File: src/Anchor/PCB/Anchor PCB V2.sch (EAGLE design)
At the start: 39 parts, among them IC1 DWM1000, IC3 ENC28J60-I_SS, J1 SI-50154-F, J2 ISP PROG 1, J3 ISP PROG 2, J4 POWER_JACK, Y1 8MHz, Y2 8MHz, Y3 25MHz

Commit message: Edited Anchor PCB schematic + Board V1
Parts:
- removed IC1: DWM1000, DWM1000:DWM1000
- added C10, C11: 100nF, rcl:C-EUC0805
- added D1: POWER, SparkFun-LED:LED-BLUE1206
- added D2: STATUS, SparkFun-LED:LED-RED1206
- added D3: TX, SparkFun-LED:LED-YELLOWLILYPAD
- added D4: RX, SparkFun-LED:LED-GREEN1206
- added D5: DWM-TX, SparkFun-LED:LED-YELLOWLILYPAD
- added D6: DWM-RX, SparkFun-LED:LED-GREEN1206
- added H1, H2, H3, H4: MOUNT-HOLE3.0, holes:MOUNT-HOLE3.0
- added L1: FB_1206, rc-master-smd:FB_1206
- added R17: 470, rcl:R-EU_R1206
- added R18, R22: 220, rcl:R-EU_R1206
- added R19, R21: 270, rcl:R-EU_R1206
- added R20: 390, rcl:R-EU_R1206
- added U$2: DWM1000, Eigen Library:DWM1000-BREAKOUT
- added UART1: UART1, Eigen Library:UART-6PIN
- added UART2: UART2, Eigen Library:UART-6PIN
- C1, C2: value 0.1uF -> 100nF; device rcl:C-EUC1206 -> rcl:C-EUC0805
- C3, C4, C5, C6, C7, C8, C9: device rcl:C-EUC1206 -> rcl:C-EUC0805
- R1, R11, R12, R13, R14, R15, R16, R2, R7, R8, R9: device rcl:R-EU_R1206 -> rcl:R-EU_R0805
- R3, R4, R5, R6: value 50 -> 49.9
- S2: value RESET 1 -> RESET 2
- U$1: value DC-DC-STEP-DOWN-LM2596 -> DC-STEPDOWN
- Y1, Y2, Y3: device SparkFun-Clocks:CRYSTALPTH-HC49US -> SparkFun-Clocks:CRYSTALSMD-HC49UP
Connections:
- removed net E-INT: IC3.~INT, MCU1.PD2_[PCINT18]
- new net DTR1: C10.1, UART1.DTR
- new net DTR2: C11.1, UART2.DTR
- new net DW-RXLED: R22.2, U$2.RXLED
- new net DW-TXLED: R21.2, U$2.TXLED
- new net N$19: UART1.CTS
- new net N$20: D5.A, R21.1
- new net N$21: D4.A, R18.1
- new net N$22: D2.A, R20.1
- new net N$23: UART2.CTS
- new net N$24: D3.A, R19.1
- new net N$25: D6.A, R22.1
- new net N$26: D1.A, R17.1
- new net RX1: MCU1.PD0_[PCINT16], UART1.TXD
- new net RX2: MCU2.PD0_[PCINT16], UART2.TXD
- new net RX3: D4.C, MCU1.PC2_[PCINT10], MCU2.PC3_[PCINT11]
- new net STATUS: D2.C, MCU1.PC1_[PCINT9]
- new net TX1: MCU1.PD1_[PCINT17], UART1.RXD
- new net TX2: MCU2.PD1_[PCINT17], UART2.RXD
- new net TX3: D3.C, MCU1.PC3_[PCINT11], MCU2.PC2_[PCINT10]
- net CS2: now also U$2.CS; no longer IC1.SPICSN
- net DW-RST: now also U$2.RST; no longer IC1.RSTN
- net GND: now also D1.C, D5.C, D6.C, U$2.GND, UART1.GND, UART2.GND; no longer IC1.VSS_1, IC1.VSS_2, IC1.VSS_3, IC1.VSS_4, IC1.VSS_5
- net IRQ: now also U$2.IRQ; no longer IC1.IRQ/GPIO8
- net MOSI2: now also R16.1; no longer R14.1
- net N$13: now also L1.2
- net N$16: now also U$2.CLK; no longer IC1.SPIMOSI
- net N$17: now also U$2.MISO; no longer IC1.SPIMISO
- net N$18: now also U$2.MOSI; no longer IC1.SPICLK
- net RST1: now also C10.2
- net RST2: now also C11.2
- net SCK2: now also R14.1; no longer R16.1
- net VCC: now also L1.1, R17.2, R18.2, R19.2, R20.2, U$2.VCC; no longer IC1.VDD3V3_1, IC1.VDD3V3_2, IC1.VDDAON
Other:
- moved on the sheet: C7, C8, C9, IC3, R10, R11, R12, R13, R14, R15, R16, R7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

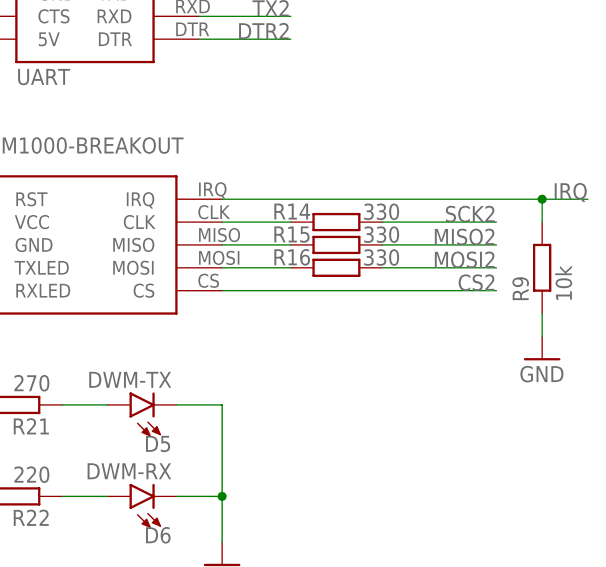
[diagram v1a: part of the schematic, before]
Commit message: Removed some unnecessary resistors in Anchor V2
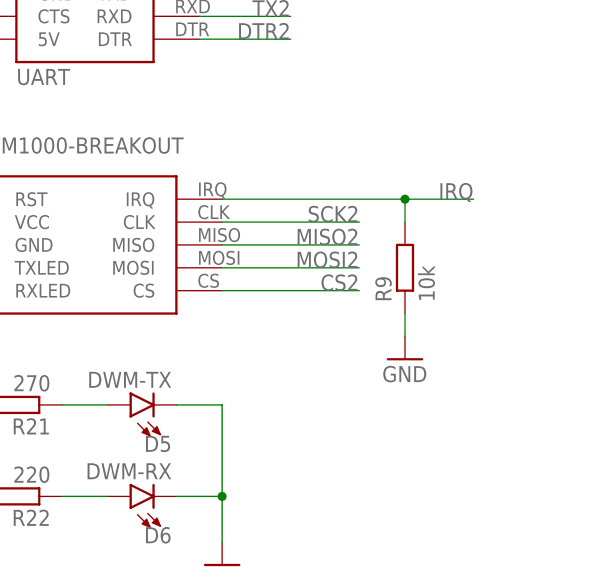
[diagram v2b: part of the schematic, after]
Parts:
- removed R14, R15, R16: 330, rcl:R-EU_R0805
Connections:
- removed net N$16: R14.2, U$2.CLK
- removed net N$17: R15.2, U$2.MISO
- removed net N$18: R16.2, U$2.MOSI
- net MISO2: now also U$2.MISO; no longer R15.1
- net MOSI2: now also U$2.MOSI; no longer R16.1
- net SCK2: now also U$2.CLK; no longer R14.1
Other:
- moved on the sheet: R9
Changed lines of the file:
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@@
 <part name="R12" library="rcl" library_urn="urn:adsk.eagle:library:334" deviceset="R-EU_" device="R0805" package3d_urn="urn:adsk.eagle:package:23553/2" value="330"/>
 <part name="R13" library="rcl" library_urn="urn:adsk.eagle:library:334" deviceset="R-EU_" device="R0805" package3d_urn="urn:adsk.eagle:package:23553/2" value="330"/>
-<part name="R14" library="rcl" library_urn="urn:adsk.eagle:library:334" deviceset="R-EU_" device="R0805" package3d_urn="urn:adsk.eagle:package:23553/2" value="330"/>
-<part name="R15" library="rcl" library_urn="urn:adsk.eagle:library:334" deviceset="R-EU_" device="R0805" package3d_urn="urn:adsk.eagle:package:23553/2" value="330"/>
-<part name="R16" library="rcl" library_urn="urn:adsk.eagle:library:334" deviceset="R-EU_" device="R0805" package3d_urn="urn:adsk.eagle:package:23553/2" value="330"/>
 <part name="J4" library="SparkFun-Connectors" deviceset="POWER_JACK" device=""/>
 <part name="U$1" library="1484249208697-powermodules" deviceset="DC-DC-STEP-DOWN-LM2596" device="" value="DC-STEPDOWN"/>
@@
 <attribute name="VALUE" x="322.58" y="78.74" size="1.778" layer="96"/>
 </instance>
-<instance part="R9" gate="G$1" x="497.84" y="137.16" rot="R90">
-<attribute name="NAME" x="496.3414" y="133.35" size="1.778" layer="95" rot="R90"/>
-<attribute name="VALUE" x="501.142" y="133.35" size="1.778" layer="96" rot="R90"/>
-</instance>
-<instance part="GND10" gate="1" x="497.84" y="127">
-<attribute name="VALUE" x="495.3" y="124.46" size="1.778" layer="96"/>
+<instance part="R9" gate="G$1" x="482.6" y="137.16" rot="R90">
+<attribute name="NAME" x="481.1014" y="133.35" size="1.778" layer="95" rot="R90"/>
+<attribute name="VALUE" x="485.902" y="133.35" size="1.778" layer="96" rot="R90"/>
+</instance>
+<instance part="GND10" gate="1" x="482.6" y="127">
+<attribute name="VALUE" x="480.06" y="124.46" size="1.778" layer="96"/>
 </instance>
 <instance part="C7" gate="G$1" x="10.16" y="116.84" rot="R180">
@@
 <attribute name="NAME" x="43.18" y="108.7374" size="1.778" layer="95" rot="R180"/>
 <attribute name="VALUE" x="32.512" y="108.712" size="1.778" layer="96" rot="R180"/>
-</instance>
-<instance part="R14" gate="G$1" x="474.98" y="142.24" rot="R180">
-<attribute name="NAME" x="472.186" y="144.2974" size="1.778" layer="95" rot="R180"/>
-<attribute name="VALUE" x="482.092" y="144.272" size="1.778" layer="96" rot="R180"/>
-</instance>
-<instance part="R15" gate="G$1" x="474.98" y="139.7" rot="R180">
-<attribute name="NAME" x="472.186" y="141.7574" size="1.778" layer="95" rot="R180"/>
-<attribute name="VALUE" x="482.092" y="141.732" size="1.778" layer="96" rot="R180"/>
-</instance>
-<instance part="R16" gate="G$1" x="474.98" y="137.16" rot="R180">
-<attribute name="NAME" x="472.186" y="139.2174" size="1.778" layer="95" rot="R180"/>
-<attribute name="VALUE" x="482.092" y="139.192" size="1.778" layer="96" rot="R180"/>
 </instance>
 <instance part="J4" gate="G$1" x="60.96" y="157.48">
@@
 <pinref part="GND10" gate="1" pin="GND"/>
 <pinref part="R9" gate="G$1" pin="1"/>
-<wire x1="497.84" y1="129.54" x2="497.84" y2="132.08" width="0.1524" layer="91"/>
+<wire x1="482.6" y1="129.54" x2="482.6" y2="132.08" width="0.1524" layer="91"/>
 </segment>
 <segment>
@@
 </segment>
 <segment>
-<pinref part="R16" gate="G$1" pin="1"/>
-<wire x1="480.06" y1="137.16" x2="492.76" y2="137.16" width="0.1524" layer="91"/>
-<label x="492.76" y="137.16" size="1.778" layer="95" rot="MR0"/>
+<label x="477.52" y="137.16" size="1.778" layer="95" rot="MR0"/>
+<pinref part="U$2" gate="G$1" pin="MOSI"/>
+<wire x1="462.28" y1="137.16" x2="477.52" y2="137.16" width="0.1524" layer="91"/>
 </segment>
 </net>
@@
 </segment>
 <segment>
-<pinref part="R15" gate="G$1" pin="1"/>
-<wire x1="480.06" y1="139.7" x2="492.76" y2="139.7" width="0.1524" layer="91"/>
-<label x="492.76" y="139.7" size="1.778" layer="95" rot="MR0"/>
+<label x="477.52" y="139.7" size="1.778" layer="95" rot="MR0"/>
+<pinref part="U$2" gate="G$1" pin="MISO"/>
+<wire x1="462.28" y1="139.7" x2="477.52" y2="139.7" width="0.1524" layer="91"/>
 </segment>
 </net>
@@
 </segment>
 <segment>
-<pinref part="R14" gate="G$1" pin="1"/>
-<wire x1="480.06" y1="142.24" x2="492.76" y2="142.24" width="0.1524" layer="91"/>
-<label x="492.76" y="142.24" size="1.778" layer="95" rot="MR0"/>
+<label x="477.52" y="142.24" size="1.778" layer="95" rot="MR0"/>
+<pinref part="U$2" gate="G$1" pin="CLK"/>
+<wire x1="462.28" y1="142.24" x2="477.52" y2="142.24" width="0.1524" layer="91"/>
 </segment>
 </net>
@@
 <segment>
 <pinref part="U$2" gate="G$1" pin="IRQ"/>
-<wire x1="462.28" y1="144.78" x2="497.84" y2="144.78" width="0.1524" layer="91"/>
+<wire x1="462.28" y1="144.78" x2="482.6" y2="144.78" width="0.1524" layer="91"/>
 <pinref part="R9" gate="G$1" pin="2"/>
-<wire x1="497.84" y1="142.24" x2="497.84" y2="144.78" width="0.1524" layer="91"/>
-<junction x="497.84" y="144.78"/>
-<wire x1="497.84" y1="144.78" x2="502.92" y2="144.78" width="0.1524" layer="91"/>
-<label x="502.92" y="144.78" size="1.778" layer="95" rot="MR0"/>
+<wire x1="482.6" y1="142.24" x2="482.6" y2="144.78" width="0.1524" layer="91"/>
+<junction x="482.6" y="144.78"/>
+<wire x1="482.6" y1="144.78" x2="490.22" y2="144.78" width="0.1524" layer="91"/>
+<label x="490.22" y="144.78" size="1.778" layer="95" rot="MR0"/>
 </segment>
 </net>
@@
 <segment>
 <pinref part="U$2" gate="G$1" pin="CS"/>
-<wire x1="462.28" y1="134.62" x2="492.76" y2="134.62" width="0.1524" layer="91"/>
-<label x="492.76" y="134.62" size="1.778" layer="95" rot="MR0"/>
+<wire x1="462.28" y1="134.62" x2="477.52" y2="134.62" width="0.1524" layer="91"/>
+<label x="477.52" y="134.62" size="1.778" layer="95" rot="MR0"/>
 </segment>
 </net>
@@
 </segment>
 </net>
-<net name="N$16" class="0">
-<segment>
-<pinref part="R14" gate="G$1" pin="2"/>
-<pinref part="U$2" gate="G$1" pin="CLK"/>
-<wire x1="469.9" y1="142.24" x2="462.28" y2="142.24" width="0.1524" layer="91"/>
-</segment>
-</net>
-<net name="N$17" class="0">
-<segment>
-<pinref part="R15" gate="G$1" pin="2"/>
-<pinref part="U$2" gate="G$1" pin="MISO"/>
-<wire x1="469.9" y1="139.7" x2="462.28" y2="139.7" width="0.1524" layer="91"/>
-</segment>
-</net>
-<net name="N$18" class="0">
-<segment>
-<pinref part="R16" gate="G$1" pin="2"/>
-<pinref part="U$2" gate="G$1" pin="MOSI"/>
-<wire x1="469.9" y1="137.16" x2="462.28" y2="137.16" width="0.1524" layer="91"/>
-</segment>
-</net>

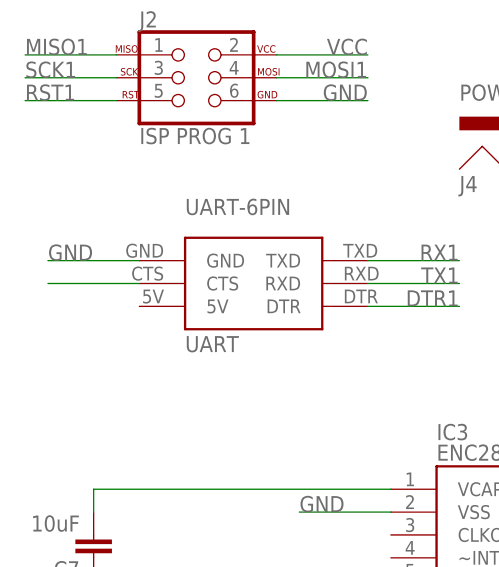
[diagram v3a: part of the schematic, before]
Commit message: Deleted CTS pin
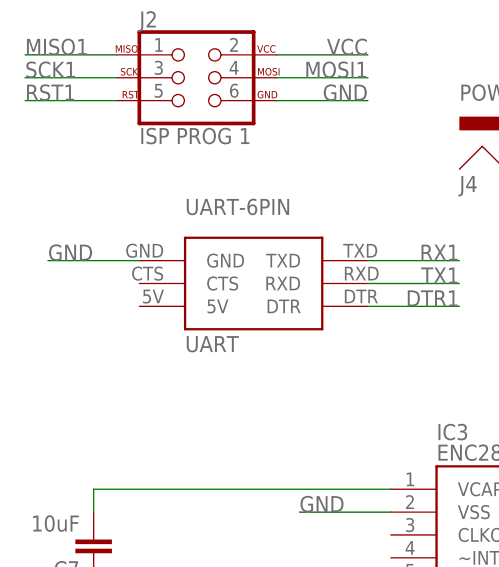
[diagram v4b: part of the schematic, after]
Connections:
- removed net N$19: UART1.CTS
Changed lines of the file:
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@@
-</segment>
-</net>
-<net name="N$19" class="0">
-<segment>
-<pinref part="UART1" gate="G$1" pin="CTS"/>
-<wire x1="15.24" y1="147.32" x2="5.08" y2="147.32" width="0.1524" layer="91"/>
 </segment>
 </net>
